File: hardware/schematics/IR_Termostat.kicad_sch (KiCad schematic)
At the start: 41 parts, among them J1 USB_C_Receptacle_PowerOnly_6P, J2 JST-PH-2mm, J3 Conn_01x03_Pin, Q1 FDN306P, SW1 SW_SPST, U1 TP4056-42-ESOP8, U2 XC6206P-3.3V, U4 MLX90614ESF-BAA-000-TU, U5 CH32V003JxMx

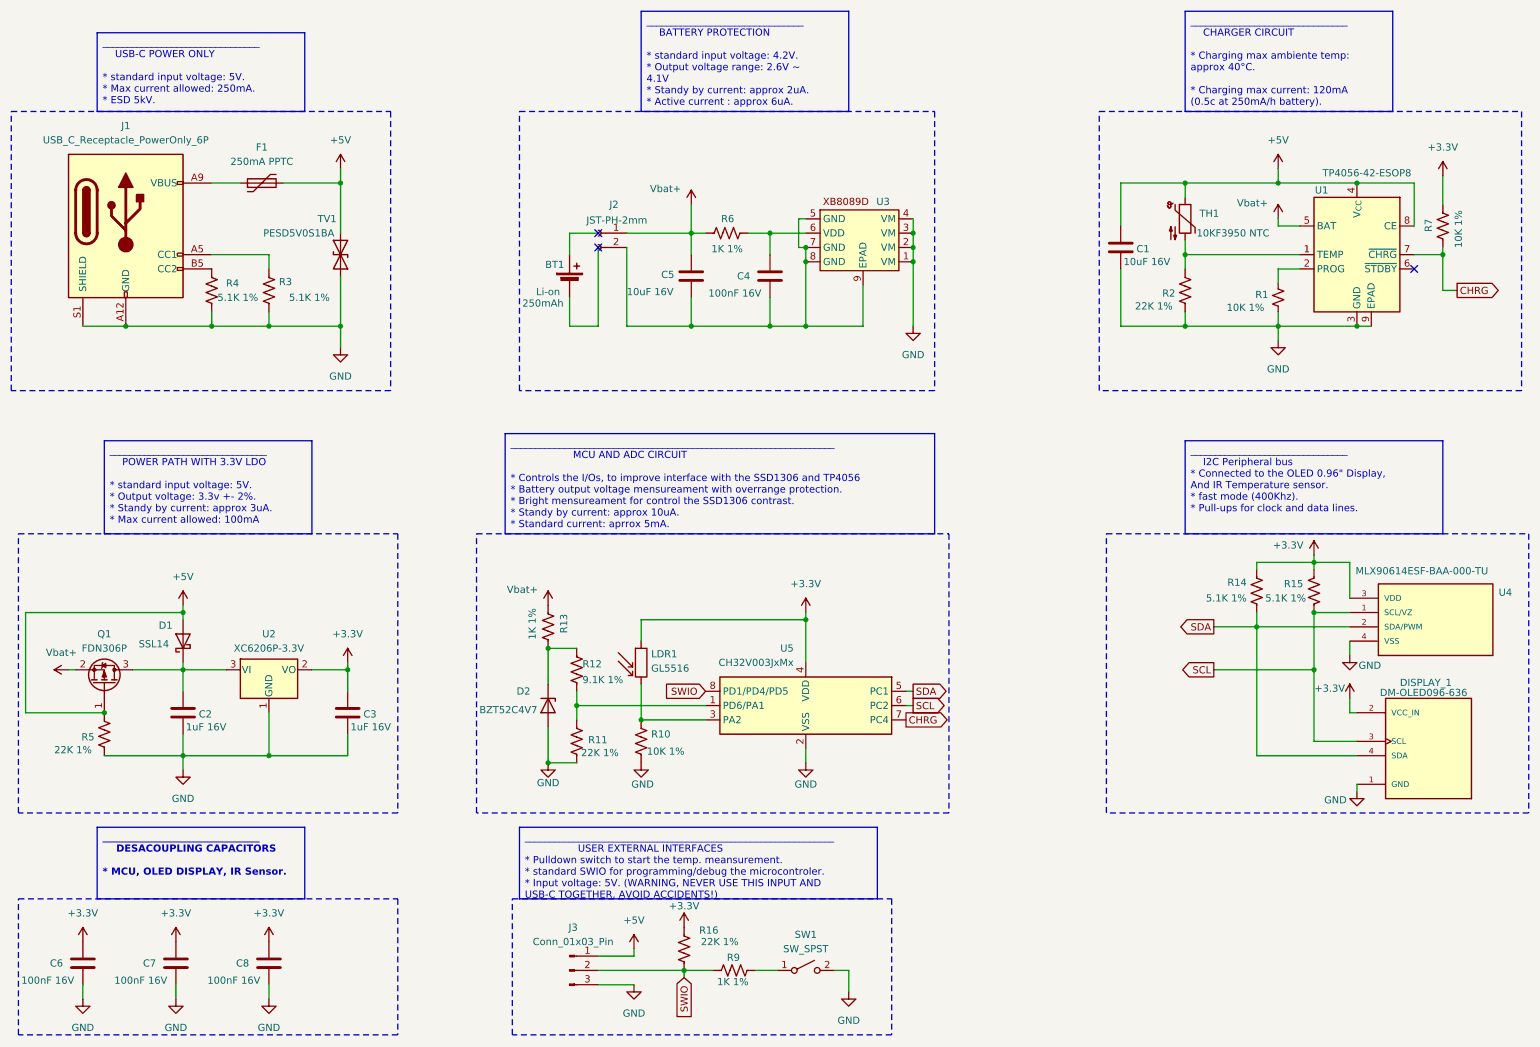
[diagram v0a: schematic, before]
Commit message: Fix: Battery mensurement circuit upgrade
Better Iq by 100x and a capacitor to filter noises, also refresh the pcb
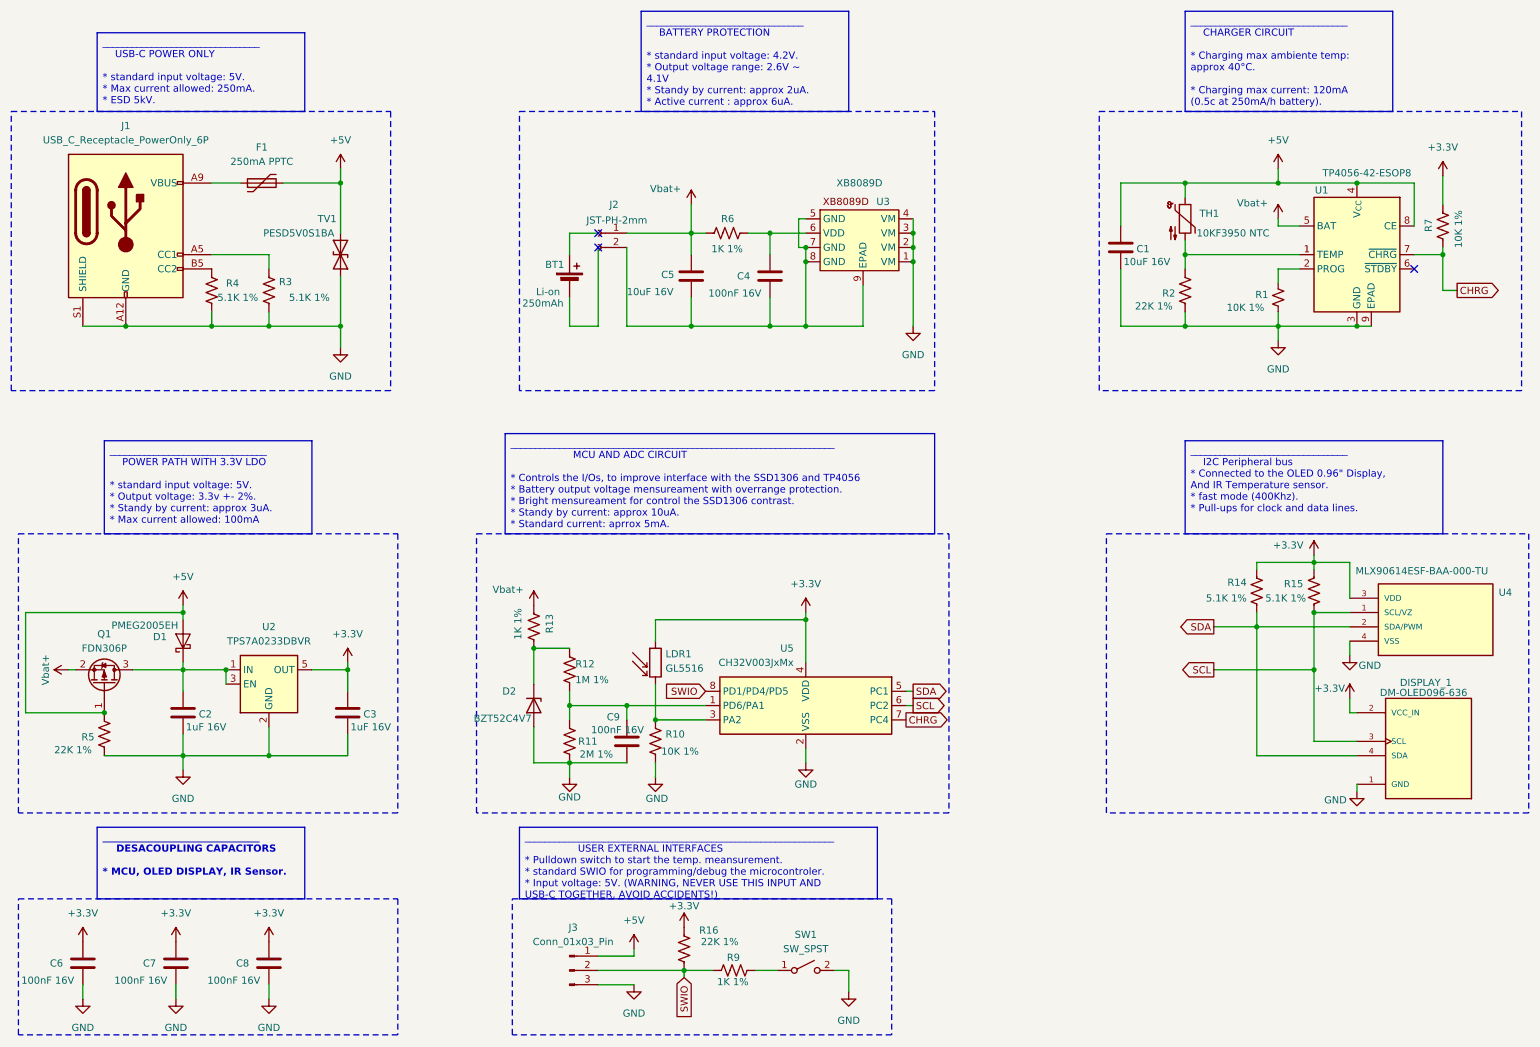
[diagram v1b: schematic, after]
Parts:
- removed D1: SSL14, Diode_SMD:D_SMA_Handsoldering, symbol Diode:SS14
- removed U2: XC6206P-3.3V, Package_TO_SOT_SMD:SOT-23-3, symbol Regulator_Linear:XC6206PxxxMR
- added C9: 100nF 16V, Capacitor_SMD:C_0805_2012Metric_Pad1.18x1.45mm_HandSolder, symbol Device:C
- added D1: PMEG2005EH, Diode_SMD:D_SOD-123F, symbol Diode:PMEG2005EH
- added U2: TPS7A0233DBVR, Package_TO_SOT_SMD:SOT-23-5, symbol Regulator_Linear:TPS7A0508PDBV
- R11: value 22K 1% -> 2M 1%
- R12: value 9.1K 1% -> 1M 1%
- U3: value ~ -> XB8089D
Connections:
- net +3.3V: now also U2.5 (OUT)
- net +5V: now also D1.2 (A)
- net GND: now also C9.2, U2.2 (GND)
- net at C2.1, Q1.3 (D): now also D1.1 (K), U2.1 (IN), U2.3 (EN)
- net at R11.1, R12.2, U5.1 (PD6/PA1): now also C9.1
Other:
- moved on the sheet: D2, LDR1, R10, R11, R12, R13

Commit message: Fix: LCSC Compliance
This commit fix the pcb, branching a new version v0.3, thats it's side-by-side with the LCSC DFM check
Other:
- moved on the sheet: R3
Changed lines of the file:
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@@
 	)
 	(junction
-		(at 59.69 69.85)
-		(diameter 0)
-		(color 0 0 0 0)
-	)
-	(junction
 		(at 245.11 111.76)
 		(diameter 0)
@@
 		(color 0 0 0 0)
 	)
+	(junction
+		(at 60.96 69.85)
+		(diameter 0)
+		(color 0 0 0 0)
+	)
 	(no_connect
 		(at 118.11 55.88)
@@
 	(wire
 		(pts
-			(xy 59.69 69.85) (xy 72.39 69.85)
-		)
-		(stroke
-			(width 0)
-			(type default)
-		)
-	)
-	(wire
-		(pts
 			(xy 128.27 133.35) (xy 128.27 139.7)
 		)
@@
 	(wire
 		(pts
-			(xy 59.69 57.15) (xy 59.69 59.69)
+			(xy 60.96 57.15) (xy 60.96 59.69)
 		)
 		(stroke
@@
 	(wire
 		(pts
-			(xy 49.53 57.15) (xy 59.69 57.15)
+			(xy 49.53 57.15) (xy 60.96 57.15)
 		)
 		(stroke
@@
 	(wire
 		(pts
-			(xy 49.53 69.85) (xy 59.69 69.85)
+			(xy 49.53 69.85) (xy 60.96 69.85)
 		)
 		(stroke
@@
 	(wire
 		(pts
-			(xy 59.69 67.31) (xy 59.69 69.85)
+			(xy 60.96 67.31) (xy 60.96 69.85)
 		)
 		(stroke
@@
 	(wire
 		(pts
+			(xy 60.96 69.85) (xy 72.39 69.85)
+		)
+		(stroke
+			(width 0)
+			(type default)
+		)
+	)
+	(wire
+		(pts
 			(xy 172.72 137.16) (xy 173.99 137.16)
 		)
@@
 	(symbol
 		(lib_id "Device:R_US")
-		(at 59.69 63.5 0)
+		(at 60.96 63.5 0)
 		(unit 1)
 		(exclude_from_sim no)
@@
 		(dnp no)
 		(property "Reference" "R3"
-			(at 61.468 61.976 0)
+			(at 62.738 61.976 0)
 			(effects
 				(font
@@
 		)
 		(property "Value" "5.1K 1%"
-			(at 63.246 64.77 0)
+			(at 62.738 64.77 0)
 			(effects
 				(font
@@
 		)
 		(property "Footprint" "Resistor_SMD:R_0805_2012Metric_Pad1.20x1.40mm_HandSolder"
-			(at 60.706 63.754 90)
+			(at 61.976 63.754 90)
 			(effects
 				(font
@@
 		)
 		(property "Datasheet" "~"
-			(at 59.69 63.5 0)
+			(at 60.96 63.5 0)
 			(effects
 				(font
@@
 		)
 		(property "Description" "Resistor, US symbol"
-			(at 59.69 63.5 0)
+			(at 60.96 63.5 0)
 			(effects
 				(font
@@
 		(dnp no)
 		(property "Reference" "C3"
-			(at 76.454 138.684 0)
+			(at 68.072 138.43 0)
 			(effects
 				(font
@@
 		)
 		(property "Value" "1uF 16V"
-			(at 74.168 140.97 0)
+			(at 62.484 140.462 0)
 			(effects
 				(font
